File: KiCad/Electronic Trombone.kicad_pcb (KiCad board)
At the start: 2 copper layers, 150 x 100 mm, 174 parts, among them J1 691137710002, J2 691137710003, J3 691137710003, J4 691137710002, J5 691137710002, Q1 NPN, Q2 PNP, Q3 NPN, Q4 PNP, Q5 NPN, Q6 NPN, SW1 D6R90F2LFS, SW2 D6R90F2LFS, SW3 D6R90F2LFS, SW4 SW_DPST, U1 CD74HC4051E, U10 TL074, U11 TL074, U2 TL074, U3 TL074, U4 40106, U5 TL074, U6 TL074, U7 TL074, U8 TL074, U9 TL074

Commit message: routed oscillator
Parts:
- added J6: 691137710002, Header 691137710002:691137710002, F.Cu at (195.5, 114.7)
- moved C5 332.5 mm to (131.5, 24.4)
- moved C6 332.5 mm to (131.5, 30.9)
- moved C7 332.5 mm to (131.5, 37.5)
- moved D3 332.5 mm to (120.0, 3.55)
- moved D4 332.5 mm to (120.0, 7.10)
- moved D5 332.5 mm to (120.0, 10.7)
- moved D6 332.5 mm to (120.0, 14.2)
- moved D7 332.5 mm to (120.0, 17.8)
- moved D8 332.5 mm to (120.0, 21.3)
- moved D9 332.5 mm to (120.0, 24.9)
- moved R37 332.5 mm to (150.0, 22.0)
- moved R38 332.5 mm to (150.0, 23.8)
- moved R39 332.5 mm to (150.2, 34.4)
- moved R40 332.5 mm to (150.0, 25.5)
- moved R41 332.5 mm to (120.0, 28.6)
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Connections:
- net /Power/Thaw 5 renamed /Power/Thaw 5C
- R20 pad 2: Net-(U5D-+) -> Net-(U7D-+)
- R21 pad 2: Net-(U5D-+) -> Net-(U7D-+)
- RV10 pad 1: //Oscillator/Mix In 1 -> //Oscillator/Mix In 2
- RV10 pad 3: //Oscillator/Mix In 2 -> //Oscillator/Mix In 1
- U5 pad 12: Net-(U5D-+) -> GND
- U5 pad 13: //Filter/Signal In -> /Power/Thaw 5D
- U5 pad 14: //Filter/Signal In -> /Power/Thaw 5D
- U7 pad 12: GND -> Net-(U7D-+)
- U7 pad 13: /Power/Thaw 7 -> //Filter/Signal In
- U7 pad 14: /Power/Thaw 7 -> //Filter/Signal In
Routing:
- net -9V: track 1.47 -> 291.6 mm, vias 0 -> 2
- net +9V: track 1.47 -> 221.9 mm, vias 0 -> 2
- net +5V: track 28.8 -> 195.0 mm
- net Net-(J3-Pad1): track 0.00 -> 71.3 mm
- net Net-(B1-Pad1): track 0.00 -> 49.8 mm
- net //Oscillator/Mix In 2: track 0.00 -> 49.0 mm
- net Net-(J3-Pad2): track 0.00 -> 46.3 mm
- net //Oscillator/Sch Inv In 1: track 0.00 -> 37.0 mm
- net //Oscillator/Mix In 1: track 0.00 -> 36.5 mm
- net //Oscillator/Sch Inv In 2: track 0.00 -> 33.7 mm
- net //Oscillator/Core In 1: track 0.00 -> 28.2 mm
- net //Oscillator/Core In 2: track 0.00 -> 26.7 mm
- net Net-(J3-Pad3): track 0.00 -> 23.5 mm
- net Net-(R26-Pad2): track 0.00 -> 22.3 mm
- net Net-(R27-Pad2): track 0.00 -> 14.6 mm
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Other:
- board size 150 x 100 mm -> 150 x 130 mm
- board text added: "Control Buttons Board"
- board text removed: "-Control Buttons Board Below-"

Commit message: started filter layout
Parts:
- moved C25 361.3 mm to (184.4, 78.4), turned to 180 degrees
- moved C24 349.9 mm to (173.2, 78.4), turned to 180 degrees
- moved C23 318.1 mm to (141.5, 78.7), turned to 180 degrees
- moved C22 306.7 mm to (130.1, 78.7), turned to 180 degrees
- moved D6 81.1 mm to (147.0, 90.7), turned to 90 degrees
- moved U8 74.8 mm to (175.0, 70.8)
- moved D5 74.7 mm to (147.0, 80.4), turned to 90 degrees
- moved D4 68.2 mm to (147.0, 69.8), turned to 90 degrees
- moved U7 67.3 mm to (132.0, 71.1)
- moved R40 62.8 mm to (129.2, 84.7)
- moved R42 62.8 mm to (129.2, 86.5)
- moved R45 62.8 mm to (129.2, 90.0)
- moved R47 62.8 mm to (129.2, 91.7)
- moved D3 61.8 mm to (147.0, 59.2), turned to 90 degrees
- moved R48 60.8 mm to (120.5, 97.5)
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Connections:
- net Net-(D3-A) renamed //Filter/Signal In w. +Offset
- C7 pad 2: Net-(D6-K) -> Net-(D5-K)
- D5 pad 2: Net-(D5-A) -> //Filter/Unprocessed Out
- D6 pad 1: Net-(D6-K) -> //Filter/Signal In w. -Offset
- D6 pad 2: //Filter/Unprocessed Out -> Net-(D5-K)
- D7 pad 2: Net-(D5-K) -> Net-(D7-A)
- D8 pad 1: GND -> Net-(D8-K)
- D9 pad 1: Net-(D9-K) -> GND
- D9 pad 2: Net-(D6-K) -> Net-(D8-K)
- R20 pad 2: Net-(U7D-+) -> Net-(U7A-+)
- R21 pad 2: Net-(U7D-+) -> Net-(U7A-+)
- R37 pad 1: Net-(U7B--) -> Net-(U7D--)
- R38 pad 2: Net-(U7B--) -> Net-(U7D--)
- R40 pad 1: Net-(U7B-+) -> Net-(U7D-+)
- R41 pad 1: Net-(D5-A) -> Net-(D7-A)
- R42 pad 2: Net-(U7B-+) -> Net-(U7D-+)
- R43 pad 2: Net-(D5-A) -> Net-(D7-A)
- R44 pad 2: Net-(D9-K) -> //Filter/Signal In w. -Offset
- R46 pad 1: Net-(D9-K) -> //Filter/Signal In w. -Offset
- U7 pad 1: //Filter/Processed Control -> //Filter/Signal In
- U7 pad 13: //Filter/Signal In -> Net-(U7D--)
- U7 pad 14: //Filter/Signal In -> Net-(R39-Pad2)
- U7 pad 2: //Filter/Processed Control -> //Filter/Signal In
- U7 pad 3: Net-(D5-A) -> Net-(U7A-+)
- U7 pad 5: Net-(U7B-+) -> Net-(D7-A)
- U7 pad 6: Net-(U7B--) -> //Filter/Processed Control
- U7 pad 7: Net-(R39-Pad2) -> //Filter/Processed Control
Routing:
- net Net-(C2-Pad1): track 0.00 -> 10.4 mm
- net Net-(U7D-+): track 1.90 -> 0.00 mm
- net Net-(U7A-+): track 0.00 -> 1.90 mm
- net Net-(R26-Pad2): track 22.3 -> 22.6 mm, vias 0 -> 1

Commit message: routed the filter, updated 0201 footprints to 0402
JLCPCB's economy PCBA has a footprint bottom limit of 0402 imperial
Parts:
- C12, C13, C14, C15, C16, C17, C18, C19, C20, C21, C22, C23, C24, C25, C26, C27, C28, C29, C30, C31, C32, C33: footprint Capacitor_SMD:C_0201_0603Metric -> Capacitor_SMD:C_0402_1005Metric
- R1, R10, R13, R14, R15, R16, R17, R18, R19, R2, R20, R22, R23, R24, R25, R26, R27, R28, R29, R3, R30, R33, R36, R37, R38, R4, R40, R42, R44, R45, R47, R54, R55, R57, R58, R59, R63, R64, R65, R68, R69, R70, R71, R72, R73, R74, R8: footprint Resistor_SMD:R_0201_0603Metric -> Resistor_SMD:R_0402_1005Metric
- moved U2 243.7 mm to (-51.2, 53.2)
- moved D7 98.5 mm to (116.3, 116.2)
- moved D8 98.5 mm to (116.3, 119.8)
- moved D9 98.5 mm to (116.3, 123.3)
- moved C24 43.6 mm to (130.2, 71.2)
- moved U8 43.4 mm to (132.2, 63.6)
- moved C25 43.2 mm to (141.8, 71.2)
- moved D6 38.3 mm to (169.1, 59.4), turned to 180 degrees
- moved C7 35.9 mm to (190.1, 54.8)
- moved R49 26.4 mm to (138.1, 81.9), turned to 180 degrees
- moved D5 24.2 mm to (159.2, 59.4), turned to 180 degrees
- moved R42 23.3 mm to (125.2, 63.5), turned to 180 degrees
- moved R40 20.5 mm to (125.2, 64.6)
- moved R44 20.3 mm to (125.2, 73.6)
- moved R37 20.3 mm to (125.2, 60.7)
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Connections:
- R49 pad 1: Net-(U8A--) -> Net-(U8D--)
- U8 pad 1: Net-(U8A--) -> /Power/Thaw 8
- U8 pad 12: GND -> //Filter/Unprocessed Out
- U8 pad 13: /Power/Thaw 8 -> Net-(U8D--)
- U8 pad 14: /Power/Thaw 8 -> Net-(U8D--)
- U8 pad 2: Net-(U8A--) -> /Power/Thaw 8
- U8 pad 3: //Filter/Unprocessed Out -> GND
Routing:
- net +9V: track 221.9 -> 305.7 mm
- net //Filter/Signal In w. -Offset: track 0.00 -> 54.0 mm
- net -9V: track 291.6 -> 344.0 mm
- net //Filter/Signal In: track 0.00 -> 25.5 mm
- net //Filter/Unprocessed Out: track 0.00 -> 24.5 mm
- net //Filter/Processed Control: track 0.00 -> 18.0 mm
- net Net-(D5-K): track 0.00 -> 17.8 mm
- net Net-(U8C-+): track 0.00 -> 16.1 mm
- net Net-(U7C--): track 0.00 -> 12.5 mm
- net Net-(U7A-+): track 1.90 -> 14.0 mm
- net Net-(U8B--): track 0.00 -> 11.3 mm
- net Net-(D3-K): track 0.00 -> 7.66 mm
- net //Filter/Signal In w. +Offset: track 0.00 -> 7.18 mm
- net Net-(U7D--): track 0.00 -> 3.65 mm
- net Net-(U7D-+): track 0.00 -> 3.62 mm
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
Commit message: amplifier layout and routing
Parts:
- moved R10 411.5 mm to (221.6, 160.6)
- moved R11 411.5 mm to (291.2, 93.4)
- moved R12 411.5 mm to (291.2, 97.4)
- moved R7 411.5 mm to (291.2, 85.3)
- moved R8 411.5 mm to (221.6, 158.8)
- moved R9 411.5 mm to (291.2, 89.3)
- moved U3 411.5 mm to (268.8, 143.3)
- moved C4 326.6 mm to (163.7, 73.7), turned to 90 degrees
- moved C10 323.6 mm to (223.0, 93.6)
- moved C11 323.6 mm to (211.3, 133.4)
- moved C8 323.6 mm to (211.3, 121.3)
- moved C9 323.6 mm to (211.3, 127.4)
- moved D10 323.6 mm to (211.0, 84.6)
- moved D11 323.6 mm to (211.0, 88.2)
- moved D12 323.6 mm to (211.0, 91.7)
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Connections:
- J1 pad 1: //Audio Out -> //Audio Control
- J1 pad 2: //Audio Control -> //Audio Out
- RV8 pad 1: Net-(R5-Pad2) -> GND
- RV8 pad 2: Net-(U2C-+) -> Net-(U2D-+)
- RV8 pad 3: GND -> Net-(R5-Pad2)
- U2 pad 1: //Oscillator/In -> /Power/Thaw 2
- U2 pad 10: Net-(U2C-+) -> //Audio Control
- U2 pad 12: GND -> Net-(U2D-+)
- U2 pad 13: /Power/Thaw 2 -> //Audio Out
- U2 pad 14: /Power/Thaw 2 -> //Audio Out
- U2 pad 2: //Oscillator/In -> /Power/Thaw 2
- U2 pad 3: //Audio Control -> GND
- U2 pad 8: //Audio Out -> //Oscillator/In
- U2 pad 9: //Audio Out -> //Oscillator/In
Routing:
- net +9V: track 305.7 -> 446.8 mm
- net //Oscillator/In: track 0.00 -> 139.2 mm, vias 0 -> 3
- net -9V: track 344.0 -> 451.7 mm
- net Net-(R5-Pad2): track 0.00 -> 40.9 mm
- net //Audio Out: track 0.00 -> 23.9 mm
- net //Oscillator/Core In 2: track 27.7 -> 4.89 mm
- net //Audio Control: track 0.00 -> 20.3 mm
- net Net-(U2D-+): track 0.00 -> 19.8 mm
- net Net-(U2B--): track 0.00 -> 17.4 mm
- net Net-(U8D--): track 2.54 -> 19.1 mm
- net Net-(U6A--): track 0.00 -> 13.8 mm
- net Net-(Q6-C): track 0.00 -> 11.8 mm
- net Net-(C4-Pad1): track 0.00 -> 11.8 mm
- net Net-(U6C-+): track 0.00 -> 11.6 mm
- net Net-(Q5-C): track 0.00 -> 11.4 mm
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
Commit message: placed missing decoupling caps next to ICs
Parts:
- moved C14 462.0 mm to (281.5, 145.1)
- moved C15 462.0 mm to (281.5, 146.8)
- moved C28 441.2 mm to (253.5, 121.2)
- moved C29 441.2 mm to (253.5, 123.0)
- moved C26 420.0 mm to (243.5, 130.5)
- moved C27 420.0 mm to (243.5, 132.2)
- moved C13 356.9 mm to (177.6, 71.2), turned to 180 degrees
- moved C12 345.1 mm to (165.8, 71.3), turned to 180 degrees
- moved C21 335.0 mm to (158.1, 71.3), turned to 180 degrees
- moved C20 323.3 mm to (146.4, 71.1), turned to 180 degrees
- moved R11 68.4 mm to (257.3, 152.8)
- moved R9 68.4 mm to (257.3, 148.8)
- moved R12 68.4 mm to (257.3, 156.8)
- moved R7 68.4 mm to (257.3, 144.7)
- moved R10 60.2 mm to (281.4, 153.0)
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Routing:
- net Net-(D7-A): track 0.00 -> 16.1 mm
- net //Amplifier/Out: track 2.54 -> 17.5 mm
- net Net-(C4-Pad1): track 11.8 -> 16.5 mm
- net -9V: track 451.7 -> 455.4 mm
- net +9V: track 446.8 -> 450.0 mm
- net Net-(D8-K): track 0.00 -> 2.60 mm
- net Net-(U6C-+): track 11.6 -> 9.11 mm
- net Net-(D7-K): track 0.00 -> 2.25 mm
- net Net-(U6D-+): track 9.48 -> 11.7 mm
- net Net-(Q5-C): track 11.4 -> 12.9 mm
- net Net-(U6C--): track 7.65 -> 8.57 mm
- net Net-(U6A--): track 13.8 -> 14.7 mm

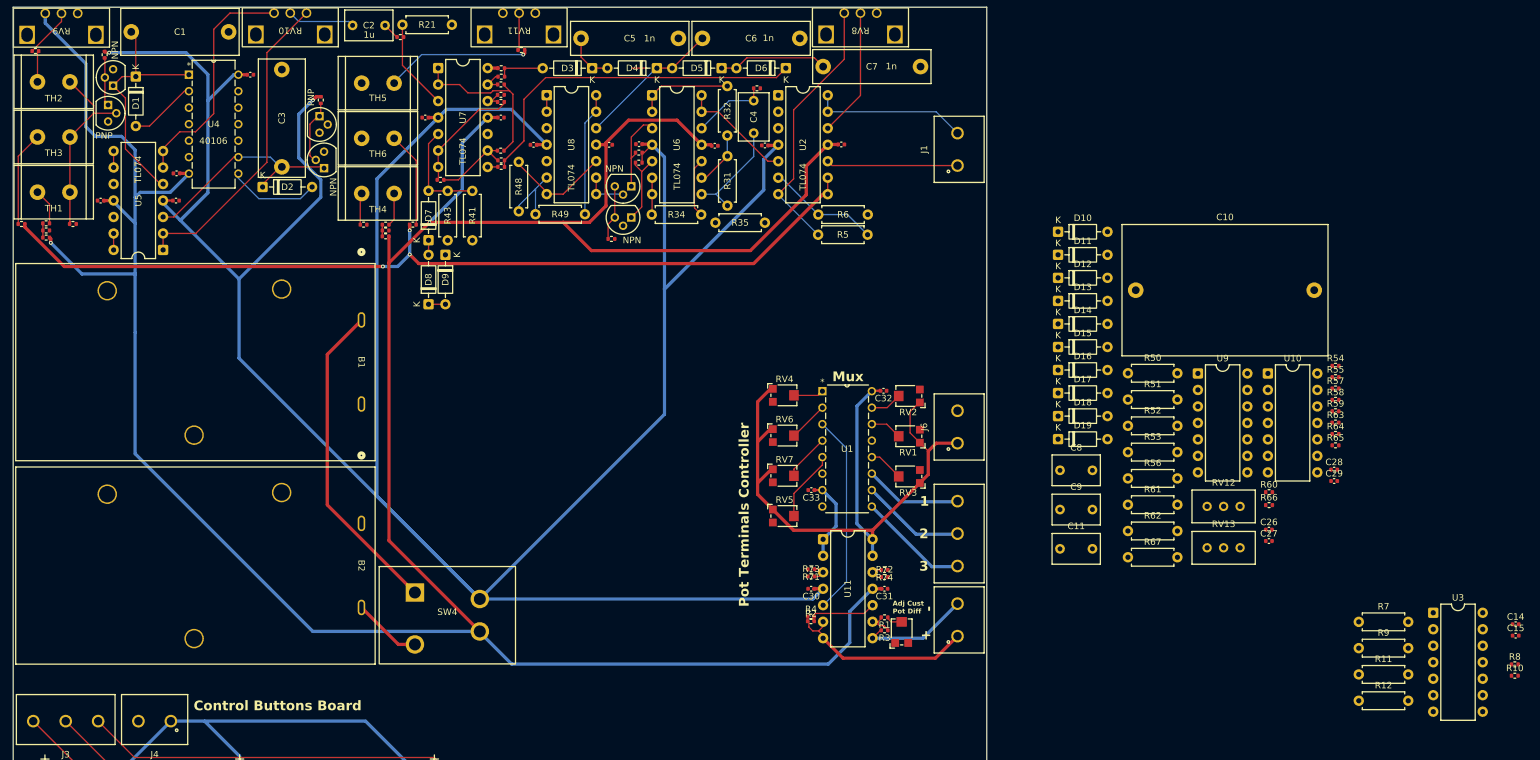
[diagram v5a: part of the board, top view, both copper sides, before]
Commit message: placed and routed envelope core
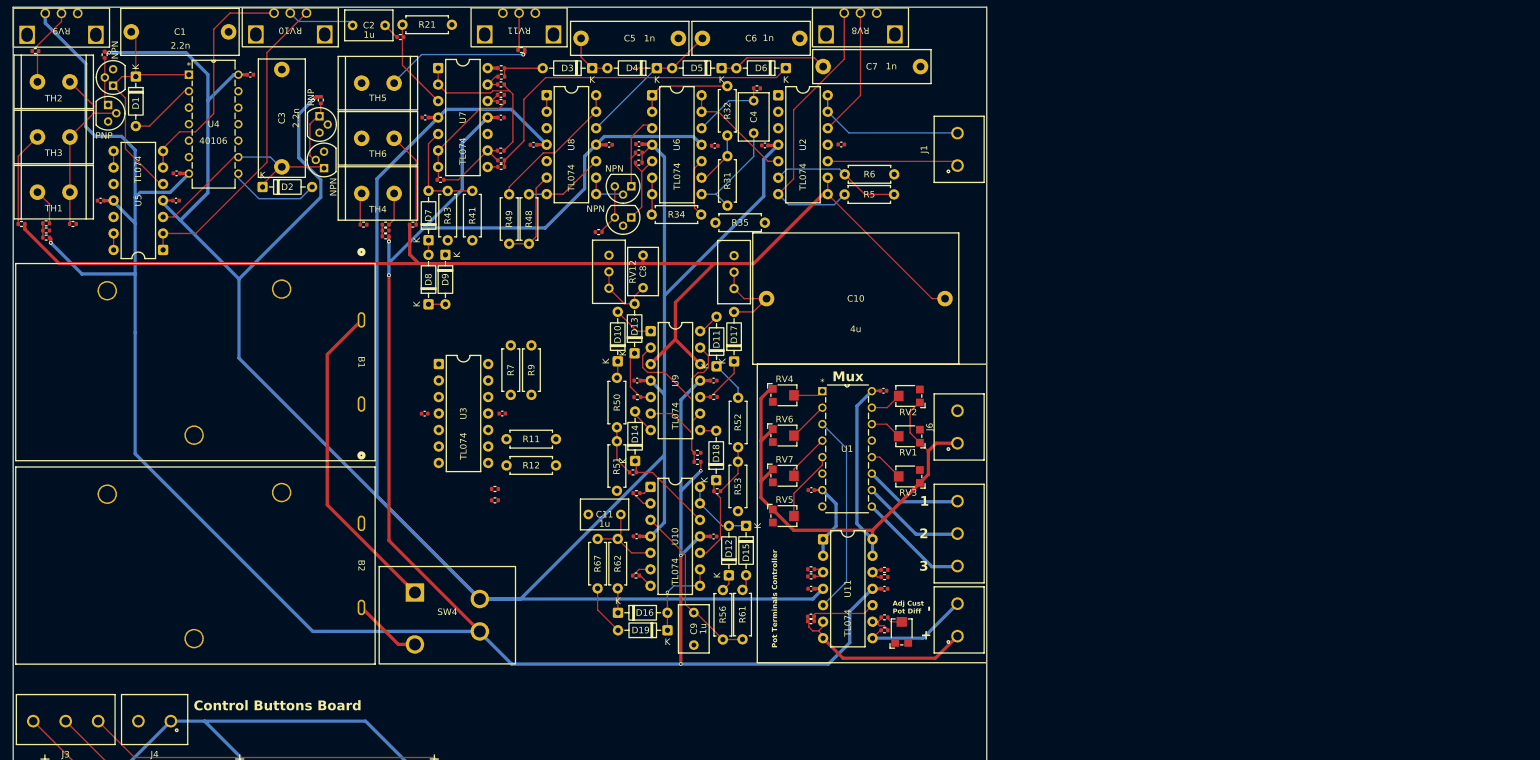
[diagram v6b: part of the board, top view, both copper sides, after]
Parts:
- removed R57, R63: 510, Resistor_SMD:R_0402_1005Metric
- moved C14 171.2 mm to (113.4, 112.6), turned to 180 degrees
- moved C15 159.8 mm to (125.4, 112.6), turned to 180 degrees
- moved R10 159.4 mm to (124.2, 126.0)
- moved R8 159.4 mm to (124.2, 124.2)
- moved U3 157.9 mm to (115.6, 105.0)
- moved R7 137.4 mm to (126.7, 102.1), turned to -90 degrees
- moved R11 136.2 mm to (126.0, 116.5)
- moved R12 136.2 mm to (126.0, 120.6)
- moved R9 133.3 mm to (129.8, 109.7), turned to 90 degrees
- moved R59 108.6 mm to (145.5, 121.7), turned to 180 degrees
- moved C28 108.0 mm to (146.1, 131.5), turned to 180 degrees
- moved R58 107.6 mm to (146.2, 110.1), turned to 180 degrees
- moved RV12 102.9 mm to (141.8, 93.3), turned to -90 degrees
- moved C26 100.0 mm to (146.2, 107.5), turned to 180 degrees
- moved R54 99.2 mm to (155.4, 118.7), turned to 180 degrees
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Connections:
- C10 pad 1: //Audio Control -> //Buffered Audio Control
- C11 pad 2: Net-(U10D-+) -> Net-(U10B-+)
- C8 pad 1: //Audio Control -> //Buffered Audio Control
- C9 pad 2: Net-(U10B-+) -> Net-(U10A-+)
- R10 pad 2: Net-(U3C-+) -> Net-(U3A-+)
- R11 pad 1: Net-(U3B-+) -> Net-(U3D-+)
- R12 pad 2: Net-(U3B-+) -> Net-(U3D-+)
- R18 pad 1: //Oscillator/In -> //Buffered Audio Control
- R27 pad 1: //Oscillator/In -> //Buffered Audio Control
- R50 pad 2: //Envelope Generator/Sustain Voltage Amp -> //Envelope Generator/Amp Sustain Voltage
- R51 pad 1: //Envelope Generator/Sustain Voltage Amp -> //Envelope Generator/Amp Sustain Voltage
- R52 pad 2: //Envelope Generator/Sustain Voltage Filter -> //Envelope Generator/Filter Sustain Voltage
- R53 pad 1: //Envelope Generator/Sustain Voltage Filter -> //Envelope Generator/Filter Sustain Voltage
- R56 pad 2: Net-(U10B-+) -> Net-(U10A-+)
- R59 pad 2: //Envelope Generator/Sustain Voltage Filter -> //Envelope Generator/Amp Sustain Voltage
- R61 pad 2: Net-(U10B-+) -> Net-(U10A-+)
- R62 pad 2: Net-(U10D-+) -> Net-(U10B-+)
- R65 pad 2: //Envelope Generator/Sustain Voltage Amp -> //Envelope Generator/Filter Sustain Voltage
- R67 pad 2: Net-(U10D-+) -> Net-(U10B-+)
- R7 pad 1: Net-(U3A-+) -> Net-(U3C-+)
- R8 pad 1: Net-(U3C-+) -> Net-(U3A-+)
- R9 pad 2: Net-(U3A-+) -> Net-(U3C-+)
- RV12 pad 1: Net-(R57-Pad2) -> Net-(D13-A)
- RV12 pad 2: Net-(R57-Pad2) -> Net-(D13-A)
- RV13 pad 1: Net-(R63-Pad2) -> Net-(D17-A)
- RV13 pad 2: Net-(R63-Pad2) -> Net-(D17-A)
- U10 pad 1: Net-(D12-A) -> Net-(R60-Pad1)
- U10 pad 12: Net-(U10D-+) -> Net-(D14-K)
- U10 pad 13: //Envelope Generator/Out Filter -> Net-(D12-A)
- U10 pad 14: Net-(R66-Pad1) -> Net-(D12-A)
- U10 pad 2: Net-(D12-A) -> //Envelope Generator/Out Amp
- U10 pad 3: Net-(D14-K) -> Net-(U10A-+)
- U10 pad 6: //Envelope Generator/Out Amp -> //Envelope Generator/Out Filter
- U10 pad 7: Net-(R60-Pad1) -> Net-(R66-Pad1)
- U2 pad 8: //Oscillator/In -> //Buffered Audio Control
- U2 pad 9: //Oscillator/In -> //Buffered Audio Control
- U3 pad 1: Net-(R10-Pad1) -> //Filter Control
- U3 pad 12: GND -> Net-(U3D-+)
- U3 pad 13: /Power/Thaw 3 -> GND
- U3 pad 14: /Power/Thaw 3 -> //Amp Control
- U3 pad 5: Net-(U3B-+) -> GND
- U3 pad 6: GND -> /Power/Thaw 3
- U3 pad 7: //Amp Control -> /Power/Thaw 3
- U3 pad 8: //Filter Control -> Net-(R10-Pad1)
- U9 pad 1: Net-(D14-A) -> Net-(D10-A)
- U9 pad 10: //Audio Control -> Net-(D17-K)
- U9 pad 12: Net-(D17-K) -> //Buffered Audio Control
- U9 pad 14: Net-(D18-A) -> Net-(D11-A)
- U9 pad 3: Net-(D13-K) -> //Buffered Audio Control
- U9 pad 5: //Audio Control -> Net-(D13-K)
- U9 pad 7: Net-(D11-A) -> Net-(D14-A)
- U9 pad 8: Net-(D10-A) -> Net-(D18-A)
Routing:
- net //Buffered Audio Control: track 0.00 -> 191.2 mm
- net //Oscillator/In: track 139.6 -> 0.00 mm, vias 3 -> 0
- net //Envelope Generator/Trigger Ref: track 0.00 -> 42.4 mm
- net Net-(U10A-+): track 0.00 -> 26.3 mm
- net +9V: track 450.0 -> 474.4 mm
- net Net-(D14-K): track 0.00 -> 14.7 mm
- net Net-(D17-A): track 0.00 -> 14.0 mm
- net Net-(D16-A): track 0.00 -> 13.8 mm, vias 0 -> 1
- net Net-(D18-K): track 0.00 -> 13.7 mm
- net Net-(U10B-+): track 0.00 -> 13.0 mm
- net Net-(D12-A): track 0.00 -> 11.1 mm
- net Net-(D13-A): track 0.00 -> 10.5 mm
- net Net-(D13-K): track 0.00 -> 9.23 mm
- net Net-(D17-K): track 0.00 -> 8.58 mm
- net //Envelope Generator/Filter Sustain Voltage: track 0.00 -> 7.90 mm
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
